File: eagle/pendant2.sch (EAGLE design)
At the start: 7 parts, among them U1 TINY85-20-DIP

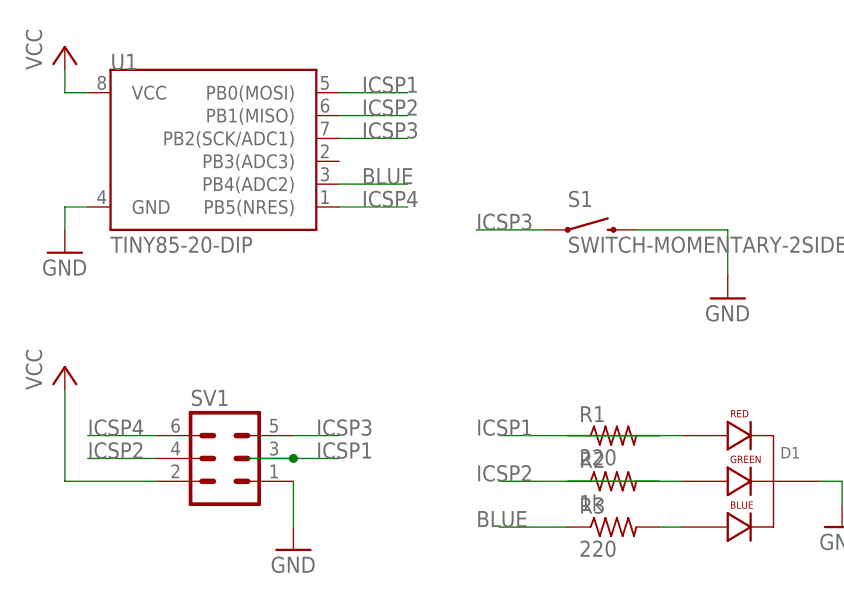
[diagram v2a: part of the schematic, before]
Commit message: redone routes and replaced resistor type
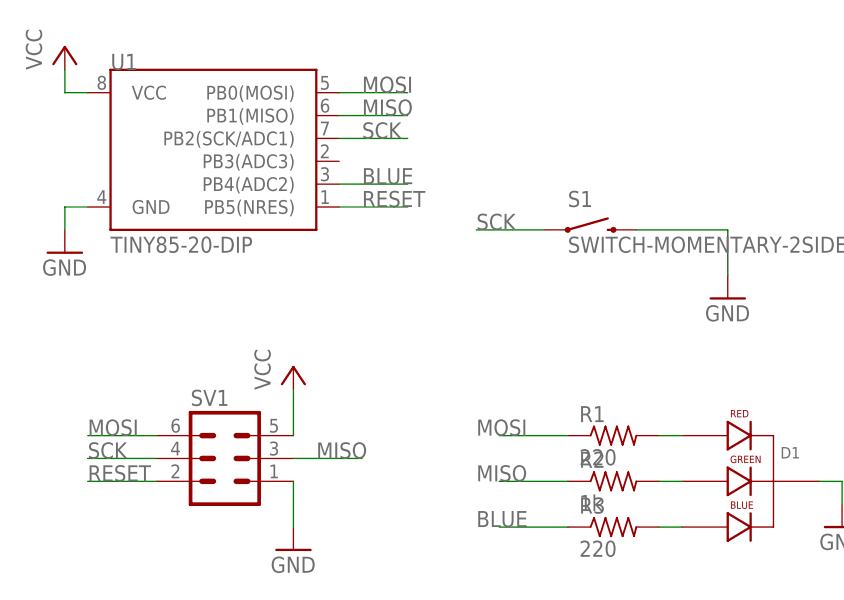
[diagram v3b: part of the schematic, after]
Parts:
- R1, R2, R3: device rcl:R-US_0411/3V -> resistor:R-US_0207/2V
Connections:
- removed net ICSP1: R1.2, SV1.3, U1.PB0(MOSI)
- removed net ICSP2: R2.2, SV1.4, U1.PB1(MISO)
- removed net ICSP3: S1.1, SV1.5, U1.PB2(SCK/ADC1)
- removed net ICSP4: SV1.6, U1.PB5(NRES)
- new net MISO: R2.1, SV1.3, U1.PB1(MISO)
- new net MOSI: R1.1, SV1.6, U1.PB0(MOSI)
- new net RESET: SV1.2, U1.PB5(NRES)
- new net SCK: S1.1, SV1.4, U1.PB2(SCK/ADC1)
- net N$1: now also R1.2; no longer R1.1
- net N$2: now also R2.2; no longer R2.1
- net VCC: now also SV1.5; no longer SV1.2
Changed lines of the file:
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@@
 <part name="GND4" library="supply1" deviceset="GND" device=""/>
 <part name="P+1" library="supply1" deviceset="VCC" device=""/>
-<part name="P+2" library="supply1" deviceset="VCC" device=""/>
 <part name="D1" library="SparkFun-LED" deviceset="LED-RGB-CC-THRU" device="CLEAR"/>
 <part name="SV1" library="con-lstb" deviceset="MA03-2" device=""/>
-<part name="R1" library="rcl" deviceset="R-US_" device="0411/3V" value="220"/>
-<part name="R2" library="rcl" deviceset="R-US_" device="0411/3V" value="1k"/>
-<part name="R3" library="rcl" deviceset="R-US_" device="0411/3V" value="220"/>
+<part name="R1" library="resistor" deviceset="R-US_" device="0207/2V" value="220"/>
+<part name="R2" library="resistor" deviceset="R-US_" device="0207/2V" value="1k"/>
+<part name="R3" library="resistor" deviceset="R-US_" device="0207/2V" value="220"/>
 <part name="S1" library="SparkFun-Electromechanical" deviceset="SWITCH-MOMENTARY-2" device="SIDE_EZ"/>
 <part name="U1" library="SparkFun-DigitalIC" deviceset="ATTINY45" device="TINY85-20-DIP" value="TINY85-20-DIP"/>
+<part name="P+2" library="supply1" deviceset="VCC" device=""/>
 </parts>
 <sheets>
@@
 <instance part="GND4" gate="1" x="33.02" y="5.08"/>
 <instance part="P+1" gate="VCC" x="7.62" y="60.96"/>
-<instance part="P+2" gate="VCC" x="7.62" y="25.4"/>
 <instance part="D1" gate="G$1" x="81.28" y="12.7"/>
 <instance part="SV1" gate="1" x="25.4" y="15.24"/>
@@
 <instance part="S1" gate="G$1" x="66.04" y="40.64"/>
 <instance part="U1" gate="G$1" x="25.4" y="48.26"/>
+<instance part="P+2" gate="VCC" x="33.02" y="25.4"/>
 </instances>
 <busses>
@@
 <net name="N$1" class="0">
 <segment>
-<pinref part="R1" gate="G$1" pin="1"/>
+<pinref part="R1" gate="G$1" pin="2"/>
 <pinref part="D1" gate="G$1" pin="RED_CATHODE"/>
-<wire x1="63.5" y1="17.78" x2="76.2" y2="17.78" width="0.1524" layer="91"/>
+<wire x1="73.66" y1="17.78" x2="76.2" y2="17.78" width="0.1524" layer="91"/>
 </segment>
 </net>
 <net name="N$2" class="0">
 <segment>
-<pinref part="R2" gate="G$1" pin="1"/>
+<pinref part="R2" gate="G$1" pin="2"/>
 <pinref part="D1" gate="G$1" pin="GREEN_CATHODE"/>
-<wire x1="63.5" y1="12.7" x2="76.2" y2="12.7" width="0.1524" layer="91"/>
+<wire x1="73.66" y1="12.7" x2="76.2" y2="12.7" width="0.1524" layer="91"/>
 </segment>
 </net>
@@
 </segment>
 <segment>
+<pinref part="SV1" gate="1" pin="5"/>
 <pinref part="P+2" gate="VCC" pin="VCC"/>
-<wire x1="7.62" y1="22.86" x2="7.62" y2="12.7" width="0.1524" layer="91"/>
-<pinref part="SV1" gate="1" pin="2"/>
-<wire x1="7.62" y1="12.7" x2="17.78" y2="12.7" width="0.1524" layer="91"/>
+<wire x1="33.02" y1="17.78" x2="33.02" y2="22.86" width="0.1524" layer="91"/>
 </segment>
 </net>
@@
 </segment>
 </net>
-<net name="ICSP1" class="0">
-<segment>
-<wire x1="27.94" y1="15.24" x2="33.02" y2="15.24" width="0.1524" layer="91"/>
-<label x="35.56" y="15.24" size="1.778" layer="95"/>
-<pinref part="SV1" gate="1" pin="3"/>
-<wire x1="33.02" y1="15.24" x2="38.1" y2="15.24" width="0.1524" layer="91"/>
-<junction x="33.02" y="15.24"/>
-</segment>
-<segment>
-<pinref part="R1" gate="G$1" pin="2"/>
-<wire x1="73.66" y1="17.78" x2="55.88" y2="17.78" width="0.1524" layer="91"/>
-<label x="53.34" y="17.78" size="1.778" layer="95"/>
-</segment>
-<segment>
-<pinref part="U1" gate="G$1" pin="PB0(MOSI)"/>
-<wire x1="38.1" y1="55.88" x2="45.72" y2="55.88" width="0.1524" layer="91"/>
-<label x="40.64" y="55.88" size="1.778" layer="95"/>
-</segment>
-</net>
-<net name="ICSP2" class="0">
-<segment>
-<pinref part="SV1" gate="1" pin="4"/>
-<wire x1="17.78" y1="15.24" x2="10.16" y2="15.24" width="0.1524" layer="91"/>
-<label x="10.16" y="15.24" size="1.778" layer="95"/>
-</segment>
-<segment>
-<pinref part="R2" gate="G$1" pin="2"/>
-<wire x1="73.66" y1="12.7" x2="55.88" y2="12.7" width="0.1524" layer="91"/>
-<label x="53.34" y="12.7" size="1.778" layer="95"/>
-</segment>
-<segment>
-<pinref part="U1" gate="G$1" pin="PB1(MISO)"/>
-<wire x1="38.1" y1="53.34" x2="45.72" y2="53.34" width="0.1524" layer="91"/>
-<label x="40.64" y="53.34" size="1.778" layer="95"/>
-</segment>
-</net>
-<net name="ICSP3" class="0">
-<segment>
-<pinref part="SV1" gate="1" pin="5"/>
-<wire x1="33.02" y1="17.78" x2="38.1" y2="17.78" width="0.1524" layer="91"/>
-<label x="35.56" y="17.78" size="1.778" layer="95"/>
-</segment>
-<segment>
-<pinref part="S1" gate="G$1" pin="1"/>
-<wire x1="60.96" y1="40.64" x2="53.34" y2="40.64" width="0.1524" layer="91"/>
-<label x="53.34" y="40.64" size="1.778" layer="95"/>
-</segment>
-<segment>
-<pinref part="U1" gate="G$1" pin="PB2(SCK/ADC1)"/>
-<wire x1="38.1" y1="50.8" x2="45.72" y2="50.8" width="0.1524" layer="91"/>
-<label x="40.64" y="50.8" size="1.778" layer="95"/>
-</segment>
-</net>
-<net name="ICSP4" class="0">
-<segment>
-<pinref part="SV1" gate="1" pin="6"/>
-<wire x1="17.78" y1="17.78" x2="10.16" y2="17.78" width="0.1524" layer="91"/>
-<label x="10.16" y="17.78" size="1.778" layer="95"/>
-</segment>
-<segment>
-<pinref part="U1" gate="G$1" pin="PB5(NRES)"/>
-<wire x1="38.1" y1="43.18" x2="45.72" y2="43.18" width="0.1524" layer="91"/>
-<label x="40.64" y="43.18" size="1.778" layer="95"/>
-</segment>
-</net>
 <net name="BLUE" class="0">
 <segment>
@@
 </segment>
 </net>
+<net name="RESET" class="0">
+<segment>
+<pinref part="SV1" gate="1" pin="2"/>
+<wire x1="17.78" y1="12.7" x2="10.16" y2="12.7" width="0.1524" layer="91"/>
+<label x="10.16" y="12.7" size="1.778" layer="95"/>
+</segment>
+<segment>
+<pinref part="U1" gate="G$1" pin="PB5(NRES)"/>
+<wire x1="38.1" y1="43.18" x2="45.72" y2="43.18" width="0.1524" layer="91"/>
+<label x="40.64" y="43.18" size="1.778" layer="95"/>
+</segment>
+</net>
+<net name="MOSI" class="0">
+<segment>
+<pinref part="U1" gate="G$1" pin="PB0(MOSI)"/>
+<wire x1="38.1" y1="55.88" x2="45.72" y2="55.88" width="0.1524" layer="91"/>
+<label x="40.64" y="55.88" size="1.778" layer="95"/>
+</segment>
+<segment>
+<pinref part="SV1" gate="1" pin="6"/>
+<wire x1="17.78" y1="17.78" x2="10.16" y2="17.78" width="0.1524" layer="91"/>
+<label x="10.16" y="17.78" size="1.778" layer="95"/>
+</segment>
+<segment>
+<pinref part="R1" gate="G$1" pin="1"/>
+<wire x1="63.5" y1="17.78" x2="55.88" y2="17.78" width="0.1524" layer="91"/>
+<label x="53.34" y="17.78" size="1.778" layer="95"/>
+</segment>
+</net>
+<net name="MISO" class="0">
+<segment>
+<pinref part="U1" gate="G$1" pin="PB1(MISO)"/>
+<wire x1="38.1" y1="53.34" x2="45.72" y2="53.34" width="0.1524" layer="91"/>
+<label x="40.64" y="53.34" size="1.778" layer="95"/>
+</segment>
+<segment>
+<pinref part="R2" gate="G$1" pin="1"/>
+<wire x1="63.5" y1="12.7" x2="55.88" y2="12.7" width="0.1524" layer="91"/>
+<label x="53.34" y="12.7" size="1.778" layer="95"/>
+</segment>
+<segment>
+<pinref part="SV1" gate="1" pin="3"/>
+<wire x1="33.02" y1="15.24" x2="40.64" y2="15.24" width="0.1524" layer="91"/>
+<label x="35.56" y="15.24" size="1.778" layer="95"/>
+</segment>
+</net>
+<net name="SCK" class="0">
+<segment>
+<pinref part="U1" gate="G$1" pin="PB2(SCK/ADC1)"/>
+<wire x1="38.1" y1="50.8" x2="45.72" y2="50.8" width="0.1524" layer="91"/>
+<label x="40.64" y="50.8" size="1.778" layer="95"/>
+</segment>
+<segment>
+<pinref part="SV1" gate="1" pin="4"/>
+<wire x1="17.78" y1="15.24" x2="10.16" y2="15.24" width="0.1524" layer="91"/>
+<label x="10.16" y="15.24" size="1.778" layer="95"/>
+</segment>
+<segment>
+<pinref part="S1" gate="G$1" pin="1"/>
+<wire x1="60.96" y1="40.64" x2="53.34" y2="40.64" width="0.1524" layer="91"/>
+<label x="53.34" y="40.64" size="1.778" layer="95"/>
+</segment>
+</net>

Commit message: fixing ICSP header
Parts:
- renumbered SV1 to ICSP
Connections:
- net GND: now also ICSP.6; no longer ICSP.1
- net MISO: now also ICSP.1; no longer ICSP.3
- net MOSI: now also ICSP.4; no longer ICSP.6
- net RESET: now also ICSP.5; no longer ICSP.2
- net SCK: now also ICSP.3; no longer ICSP.4
- net VCC: now also ICSP.2; no longer ICSP.5
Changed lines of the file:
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@@
 <part name="P+1" library="supply1" deviceset="VCC" device=""/>
 <part name="D1" library="SparkFun-LED" deviceset="LED-RGB-CC-THRU" device="CLEAR"/>
-<part name="SV1" library="con-lstb" deviceset="MA03-2" device=""/>
+<part name="ICSP" library="con-lstb" deviceset="MA03-2" device=""/>
 <part name="R1" library="resistor" deviceset="R-US_" device="0207/2V" value="220"/>
 <part name="R2" library="resistor" deviceset="R-US_" device="0207/2V" value="1k"/>
@@
 <instance part="P+1" gate="VCC" x="7.62" y="60.96"/>
 <instance part="D1" gate="G$1" x="81.28" y="12.7"/>
-<instance part="SV1" gate="1" x="25.4" y="15.24"/>
+<instance part="ICSP" gate="1" x="25.4" y="15.24" rot="R180"/>
 <instance part="R1" gate="G$1" x="68.58" y="17.78"/>
 <instance part="R2" gate="G$1" x="68.58" y="12.7"/>
@@
 </segment>
 <segment>
-<pinref part="SV1" gate="1" pin="5"/>
+<pinref part="ICSP" gate="1" pin="2"/>
 <pinref part="P+2" gate="VCC" pin="VCC"/>
 <wire x1="33.02" y1="17.78" x2="33.02" y2="22.86" width="0.1524" layer="91"/>
@@
 </segment>
 <segment>
-<pinref part="SV1" gate="1" pin="1"/>
+<pinref part="ICSP" gate="1" pin="6"/>
 <pinref part="GND4" gate="1" pin="GND"/>
 <wire x1="33.02" y1="12.7" x2="33.02" y2="7.62" width="0.1524" layer="91"/>
@@
 <net name="RESET" class="0">
 <segment>
-<pinref part="SV1" gate="1" pin="2"/>
+<pinref part="ICSP" gate="1" pin="5"/>
 <wire x1="17.78" y1="12.7" x2="10.16" y2="12.7" width="0.1524" layer="91"/>
 <label x="10.16" y="12.7" size="1.778" layer="95"/>
@@
 </segment>
 <segment>
-<pinref part="SV1" gate="1" pin="6"/>
-<wire x1="17.78" y1="17.78" x2="10.16" y2="17.78" width="0.1524" layer="91"/>
-<label x="10.16" y="17.78" size="1.778" layer="95"/>
-</segment>
-<segment>
 <pinref part="R1" gate="G$1" pin="1"/>
 <wire x1="63.5" y1="17.78" x2="55.88" y2="17.78" width="0.1524" layer="91"/>
 <label x="53.34" y="17.78" size="1.778" layer="95"/>
+</segment>
+<segment>
+<pinref part="ICSP" gate="1" pin="4"/>
+<wire x1="33.02" y1="15.24" x2="40.64" y2="15.24" width="0.1524" layer="91"/>
+<label x="35.56" y="15.24" size="1.778" layer="95"/>
 </segment>
 </net>
@@
 </segment>
 <segment>
-<pinref part="SV1" gate="1" pin="3"/>
-<wire x1="33.02" y1="15.24" x2="40.64" y2="15.24" width="0.1524" layer="91"/>
-<label x="35.56" y="15.24" size="1.778" layer="95"/>
+<pinref part="ICSP" gate="1" pin="1"/>
+<wire x1="17.78" y1="17.78" x2="10.16" y2="17.78" width="0.1524" layer="91"/>
+<label x="10.16" y="17.78" size="1.778" layer="95"/>
 </segment>
 </net>
@@
 </segment>
 <segment>
-<pinref part="SV1" gate="1" pin="4"/>
+<pinref part="ICSP" gate="1" pin="3"/>
 <wire x1="17.78" y1="15.24" x2="10.16" y2="15.24" width="0.1524" layer="91"/>
 <label x="10.16" y="15.24" size="1.778" layer="95"/>
